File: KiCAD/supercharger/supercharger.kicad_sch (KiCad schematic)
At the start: 25 parts, among them J2 BAT, J4 UJC-H-G-SMT-1-P6-TR, U1 STC4054, U2 HM1160

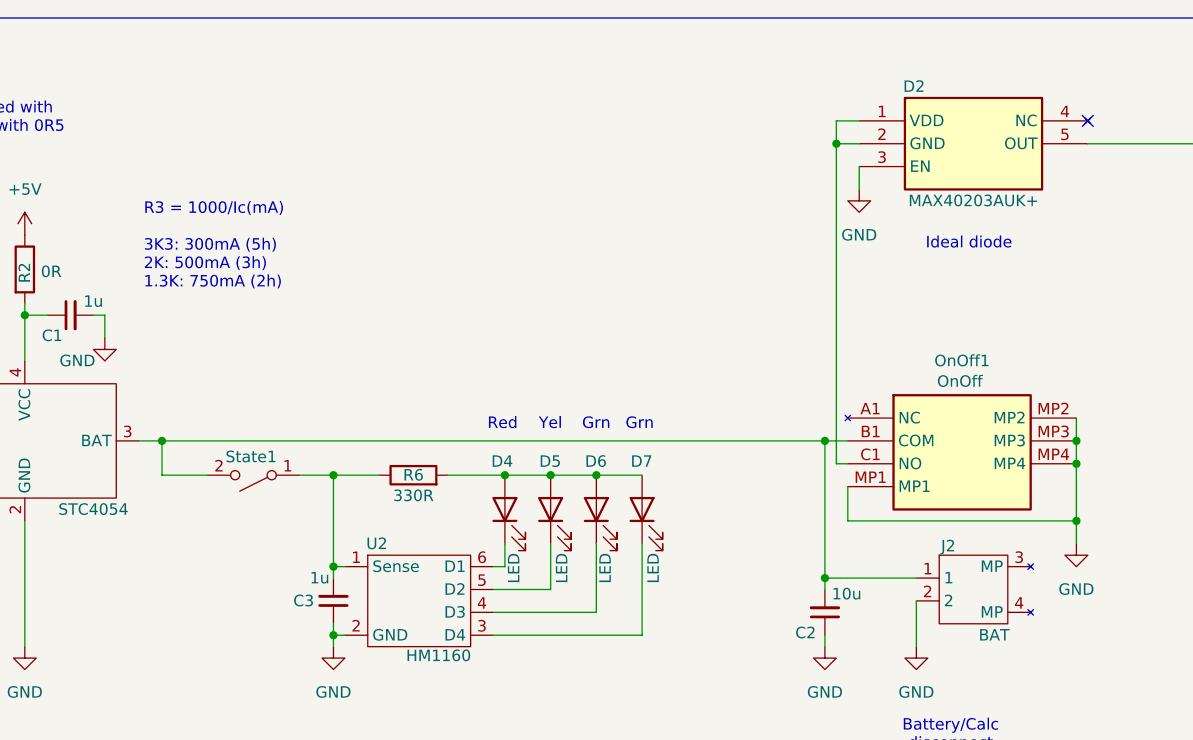
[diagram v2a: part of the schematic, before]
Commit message: PCB: Massive blunder around D2 fixed.
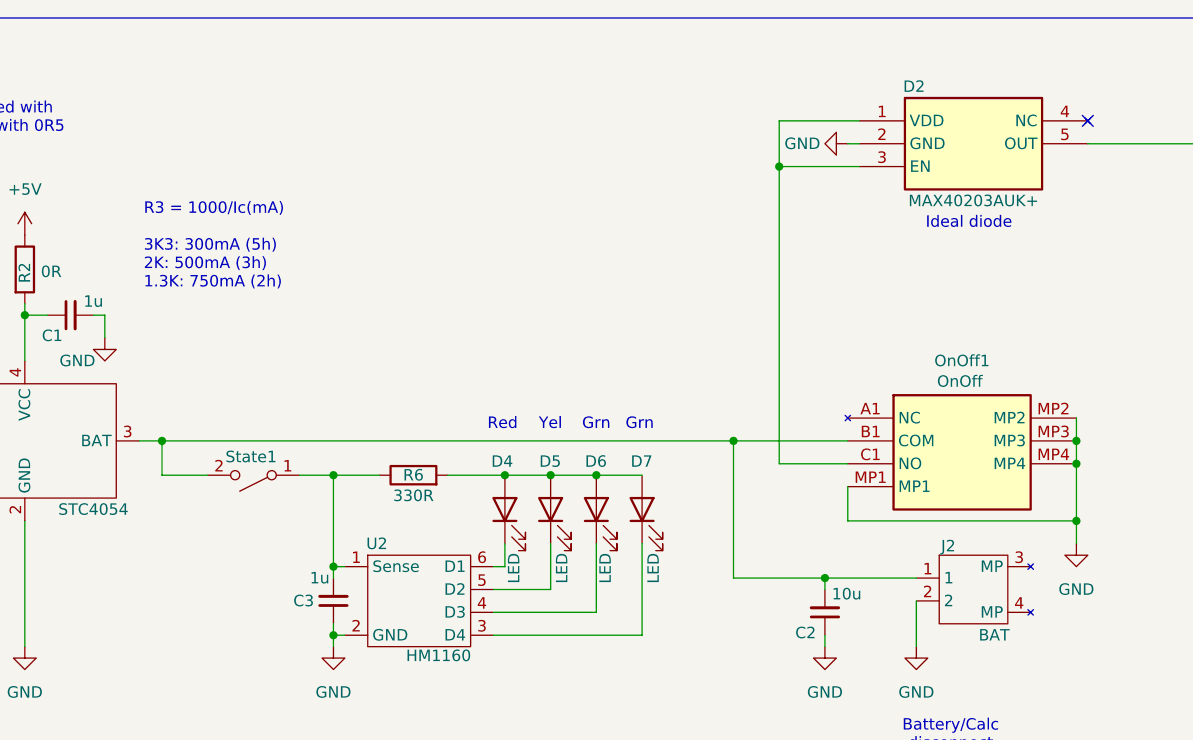
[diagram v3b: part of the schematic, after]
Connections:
- net GND: now also D2.2 (GND); no longer D2.3 (EN)
- net at D2.1 (VDD), OnOff1.C1 (NO): now also D2.3 (EN); no longer D2.2 (GND)
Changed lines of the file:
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@@
 	)
 	(junction
-		(at 144.78 34.29)
+		(at 133.35 67.31)
 		(diameter 0)
 		(color 0 0 0 0)
@@
 	)
 	(junction
+		(at 138.43 36.83)
+		(diameter 0)
+		(color 0 0 0 0)
+	)
+	(junction
 		(at 27.94 158.75)
 		(diameter 0)
@@
 	)
 	(junction
-		(at 143.51 67.31)
-		(diameter 0)
-		(color 0 0 0 0)
-	)
-	(junction
 		(at 27.94 149.86)
 		(diameter 0)
@@
 	(wire
 		(pts
-			(xy 144.78 34.29) (xy 144.78 31.75)
-		)
-		(stroke
-			(width 0)
-			(type default)
-		)
-	)
-	(wire
-		(pts
 			(xy 143.51 88.9) (xy 143.51 90.17)
 		)
@@
 	(wire
 		(pts
-			(xy 69.85 67.31) (xy 143.51 67.31)
+			(xy 69.85 67.31) (xy 133.35 67.31)
+		)
+		(stroke
+			(width 0)
+			(type default)
+		)
+	)
+	(wire
+		(pts
+			(xy 146.05 34.29) (xy 147.32 34.29)
 		)
 		(stroke
@@
 	(wire
 		(pts
-			(xy 147.32 34.29) (xy 144.78 34.29)
-		)
-		(stroke
-			(width 0)
-			(type default)
-		)
-	)
-	(wire
-		(pts
 			(xy 107.95 78.74) (xy 107.95 81.28)
 		)
@@
 	(wire
 		(pts
+			(xy 138.43 36.83) (xy 138.43 69.85)
+		)
+		(stroke
+			(width 0)
+			(type default)
+		)
+	)
+	(wire
+		(pts
 			(xy 41.91 68.58) (xy 33.02 68.58)
 		)
@@
 	(wire
 		(pts
-			(xy 144.78 34.29) (xy 144.78 69.85)
-		)
-		(stroke
-			(width 0)
-			(type default)
-		)
-	)
-	(wire
-		(pts
 			(xy 63.5 142.24) (xy 63.5 140.97)
 		)
@@
 	(wire
 		(pts
-			(xy 143.51 67.31) (xy 143.51 82.55)
+			(xy 133.35 67.31) (xy 133.35 82.55)
+		)
+		(stroke
+			(width 0)
+			(type default)
+		)
+	)
+	(wire
+		(pts
+			(xy 138.43 31.75) (xy 147.32 31.75)
 		)
 		(stroke
@@
 	(wire
 		(pts
-			(xy 147.32 36.83) (xy 147.32 39.37)
-		)
-		(stroke
-			(width 0)
-			(type default)
-		)
-	)
-	(wire
-		(pts
 			(xy 74.93 71.12) (xy 69.85 71.12)
 		)
@@
 	(wire
 		(pts
+			(xy 138.43 36.83) (xy 147.32 36.83)
+		)
+		(stroke
+			(width 0)
+			(type default)
+		)
+	)
+	(wire
+		(pts
 			(xy 27.94 147.32) (xy 27.94 149.86)
 		)
@@
 	(wire
 		(pts
+			(xy 133.35 67.31) (xy 146.05 67.31)
+		)
+		(stroke
+			(width 0)
+			(type default)
+		)
+	)
+	(wire
+		(pts
 			(xy 88.9 87.63) (xy 88.9 88.9)
 		)
@@
 	(wire
 		(pts
+			(xy 133.35 82.55) (xy 143.51 82.55)
+		)
+		(stroke
+			(width 0)
+			(type default)
+		)
+	)
+	(wire
+		(pts
 			(xy 67.31 148.59) (xy 67.31 147.32)
 		)
@@
 	(wire
 		(pts
-			(xy 144.78 31.75) (xy 147.32 31.75)
+			(xy 138.43 36.83) (xy 138.43 31.75)
 		)
 		(stroke
@@
 	(wire
 		(pts
-			(xy 146.05 69.85) (xy 144.78 69.85)
+			(xy 146.05 69.85) (xy 138.43 69.85)
 		)
 		(stroke
@@
 		(pts
 			(xy 33.02 68.58) (xy 33.02 72.39)
-		)
-		(stroke
-			(width 0)
-			(type default)
-		)
-	)
-	(wire
-		(pts
-			(xy 143.51 67.31) (xy 146.05 67.31)
 		)
 		(stroke
@@
 	(text "Ideal diode"
 		(exclude_from_sim no)
-		(at 159.512 45.466 0)
+		(at 159.512 43.18 0)
 		(effects
 			(font
@@
 	(symbol
 		(lib_id "power:GND")
-		(at 147.32 39.37 0)
+		(at 146.05 34.29 270)
 		(unit 1)
 		(exclude_from_sim no)
@@
 		(on_board yes)
 		(dnp no)
-		(fields_autoplaced yes)
 		(property "Reference" "#PWR016"
-			(at 147.32 45.72 0)
+			(at 139.7 34.29 0)
 			(effects
 				(font
@@
 		)
 		(property "Value" "GND"
-			(at 147.32 44.45 0)
-			(effects
-				(font
-					(size 1.27 1.27)
-				)
+			(at 143.002 34.29 90)
+			(effects
+				(font
+					(size 1.27 1.27)
+				)
+				(justify right)
 			)
 		)
 		(property "Footprint" ""
-			(at 147.32 39.37 0)
+			(at 146.05 34.29 0)
 			(effects
 				(font
@@
 		)
 		(property "Datasheet" ""
-			(at 147.32 39.37 0)
+			(at 146.05 34.29 0)
 			(effects
 				(font
@@
 		)
 		(property "Description" "Power symbol creates a global label with name \"GND\" , ground"
-			(at 147.32 39.37 0)
-			(effects
-				(font
+			(at 146.05 34.29 0)
+			(effects
+				(font
